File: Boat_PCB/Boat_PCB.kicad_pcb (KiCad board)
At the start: 2 copper layers, 95 x 102.5 mm, 4 parts, among them J1 Conn_02x06_Odd_Even

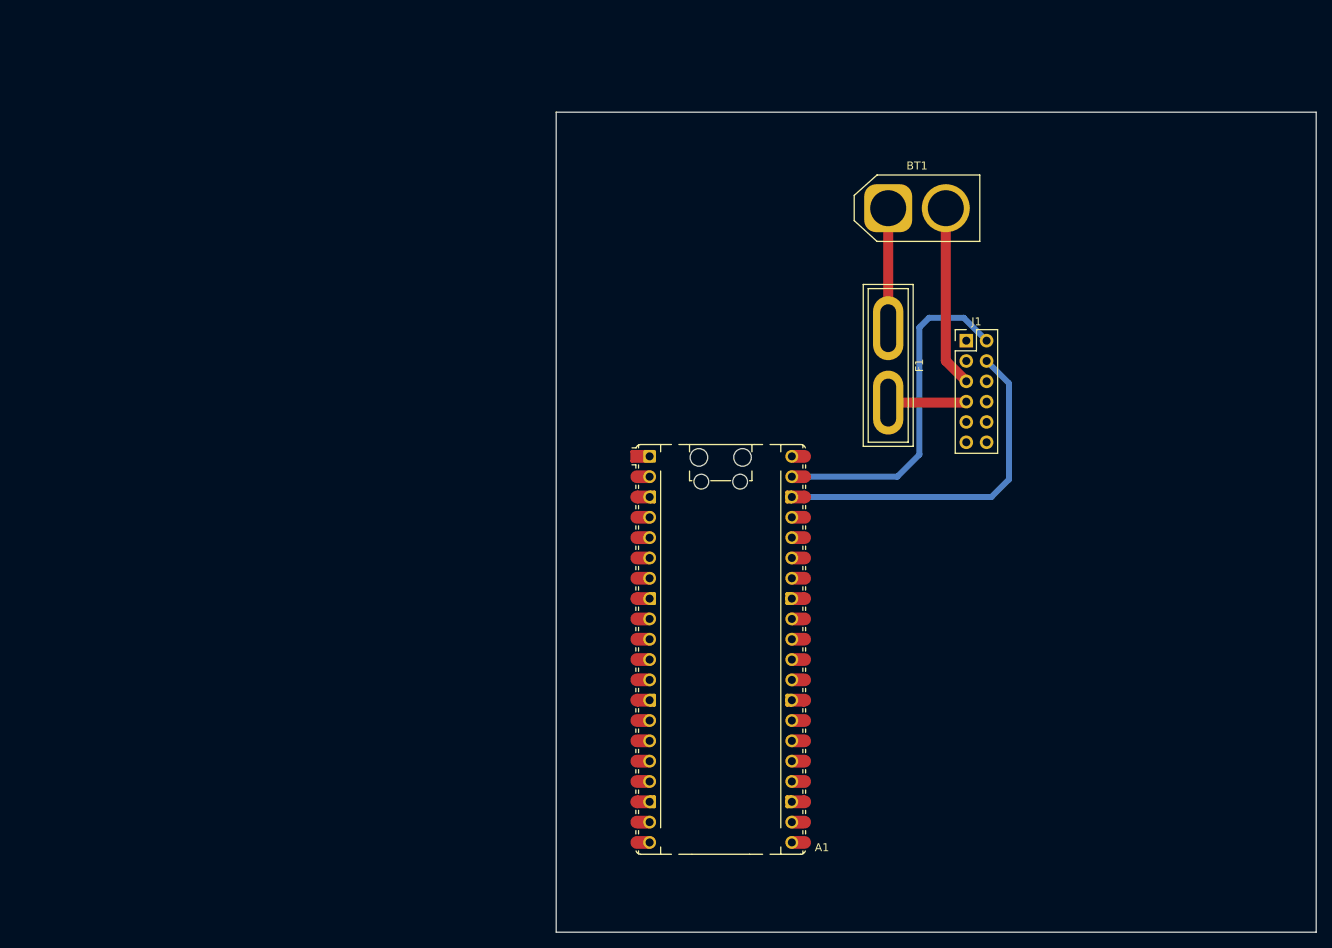
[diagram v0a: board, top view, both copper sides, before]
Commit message: Align-first steering, waypoint planner page, and M18 battery migration
Replaces proximity-boost turn logic with an align-first controller that
pivots the boat to face the next waypoint before driving forward, fixing
orbiting around waypoints. Adds a standalone waypoint planner page with a
saved-path library, wired into the command center's LOAD PATH picker and
SET HDG control. Also carries forward the three-domain Milwaukee M18
battery migration in firmware/docs and the KiCad schematic/PCB rework to
match the new divider values.

Co-Authored-By: Claude Sonnet 5 <noreply@anthropic.com>
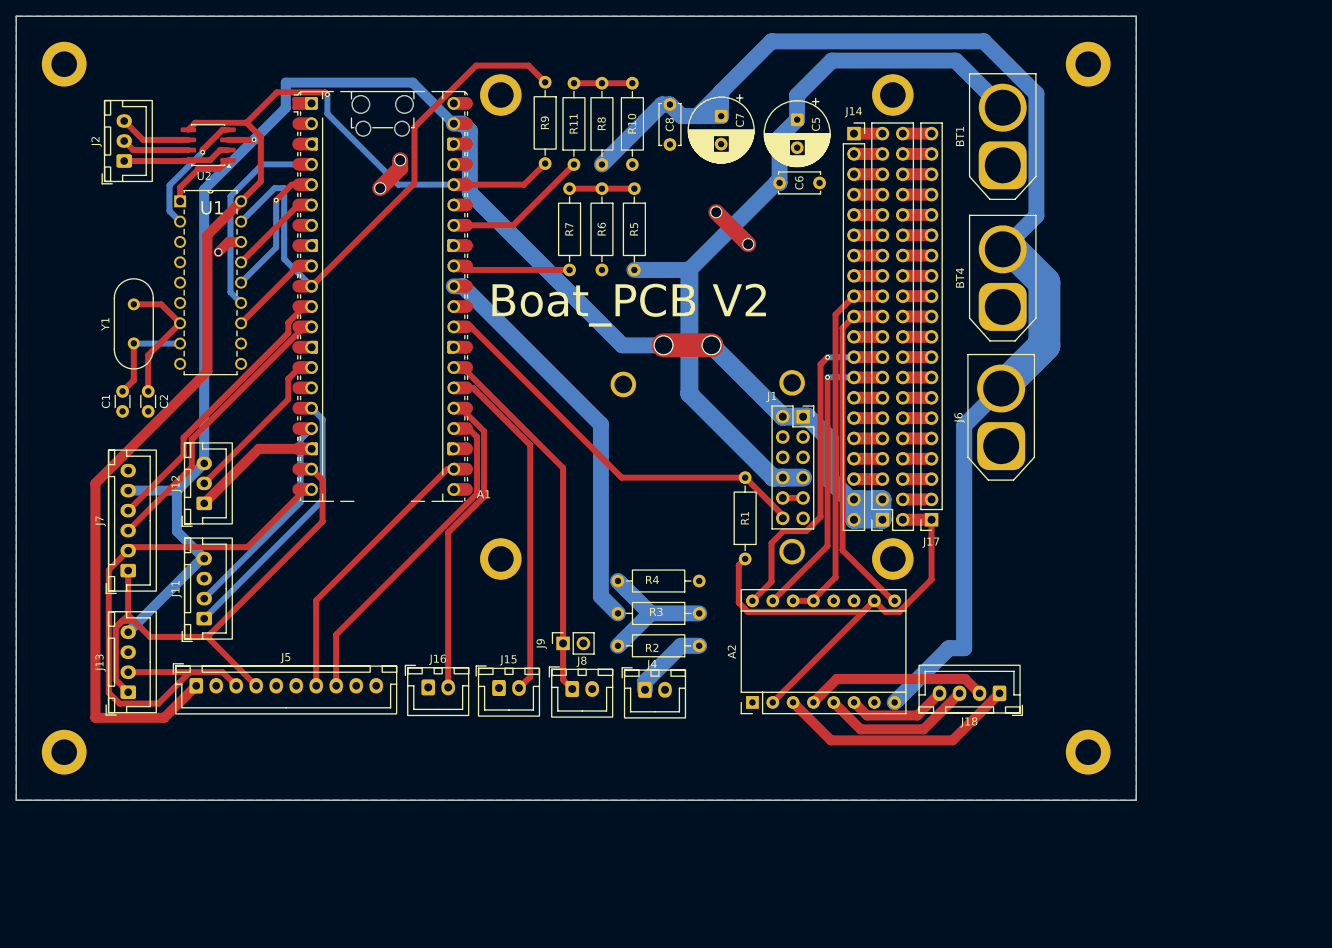
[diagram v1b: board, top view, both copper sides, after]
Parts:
- removed F1: Fuse, Fuse:Fuse_Blade_ATO_directSolder
- added A2: Pololu_Breakout_A4988, Module:Pololu_Breakout-16_15.2x20.3mm, F.Cu at (138.0, 106.8)
- added BT4: 4s, Connector_AMASS:AMASS_XT60-M_1x02_P7.20mm_Vertical, F.Cu at (169.3, 57.3)
- added C1: C, Capacitor_THT:C_Disc_D3.0mm_W1.6mm_P2.50mm, F.Cu at (59.3, 70.4)
- added C2: C, Capacitor_THT:C_Disc_D3.0mm_W1.6mm_P2.50mm, F.Cu at (62.5, 70.4)
- added C5: C_Polarized, Capacitor_THT:CP_Radial_D8.0mm_P3.50mm, F.Cu at (143.6, 33.9)
- added C6: C, Capacitor_THT:C_Disc_D5.0mm_W2.5mm_P5.00mm, F.Cu at (141.4, 41.8)
- added C7: C_Polarized, Capacitor_THT:CP_Radial_D8.0mm_P3.50mm, F.Cu at (134.1, 33.5)
- added C8: C, Capacitor_THT:C_Disc_D5.0mm_W2.5mm_P5.00mm, F.Cu at (127.7, 32.0)
- added J11: Temp + Humidity Sensor External GPIO 12,13 I2C, Connector_JST:JST_XH_B4B-XH-A_1x04_P2.50mm_Vertical, F.Cu at (69.5, 96.3)
- added J12: led GPIO 12, Connector_JST:JST_XH_B3B-XH-A_1x03_P2.50mm_Vertical, F.Cu at (69.5, 81.9)
- added J13: Temp + Humidity Sensor Internal GPIO 14,15 I2C, Connector_JST:JST_XH_B4B-XH-A_1x04_P2.50mm_Vertical, F.Cu at (60.0, 105.5)
- added J14: Conn_01x20_Socket, Connector_PinSocket_2.54mm:PinSocket_1x20_P2.54mm_Vertical, F.Cu at (150.7, 35.7)
- added J15: Hull Leak Right GPIO 20, Connector_JST:JST_XH_B2B-XH-A_1x02_P2.50mm_Vertical, F.Cu at (106.3, 105.0)
- added J16: Hull Leak Left GPIO 19, Connector_JST:JST_XH_B2B-XH-A_1x02_P2.50mm_Vertical, F.Cu at (97.5, 104.9)
- added J17: Conn_01x20_Socket, Connector_PinSocket_2.54mm:PinSocket_1x20_P2.54mm_Vertical, F.Cu at (160.4, 83.9)
- added J18: Stepper Motor, Connector_JST:JST_XH_B4B-XH-A_1x04_P2.50mm_Vertical, F.Cu at (168.9, 105.6)
- added J2: Conn_01x03_Socket, Connector_JST:JST_XH_B3B-XH-A_1x03_P2.50mm_Vertical, F.Cu at (59.5, 39.1)
- added J3: Raspberry Pi 5 connector, Module:Raspberry Pi Mounting, F.Cu at (106.6, 88.8)
- added J4: 12s Tap, Connector_JST:JST_XH_B2B-XH-A_1x02_P2.50mm_Vertical, F.Cu at (124.6, 105.2)
- added J5: IMU 14,15 I2C 17,18 RST and INT., Connector_JST:JST_XH_B10B-XH-A_1x10_P2.50mm_Vertical, F.Cu at (68.5, 104.7)
- added J6: 4s output, Connector_AMASS:AMASS_XT60-M_1x02_P7.20mm_Vertical, F.Cu at (169.1, 74.7)
- added J7: GPS + Compass GPIO 8,9 +15,14 I2C, Connector_JST:JST_XH_B6B-XH-A_1x06_P2.50mm_Vertical, F.Cu at (60.0, 90.3)
- added J8: Winch ESC GPIO 21, Connector_JST:JST_XH_B2B-XH-A_1x02_P2.50mm_Vertical, F.Cu at (115.5, 105.1)
- added J9: Winch ESC RC, Connector_PinSocket_2.54mm:PinSocket_1x02_P2.54mm_Vertical, F.Cu at (114.4, 99.4)
- added R1: R 10k, Resistor_THT:R_Axial_DIN0207_L6.3mm_D2.5mm_P10.16mm_Horizontal, F.Cu at (137.1, 88.8)
- added R10: R 18k, Resistor_THT:R_Axial_DIN0207_L6.3mm_D2.5mm_P10.16mm_Horizontal, F.Cu at (123.0, 39.5)
- added R11: R 10k, Resistor_THT:R_Axial_DIN0207_L6.3mm_D2.5mm_P10.16mm_Horizontal, F.Cu at (112.1, 29.3)
- added R2: R 220k, Resistor_THT:R_Axial_DIN0207_L6.3mm_D2.5mm_P10.16mm_Horizontal, F.Cu at (131.4, 99.7)
- added R3: R 1k, Resistor_THT:R_Axial_DIN0207_L6.3mm_D2.5mm_P10.16mm_Horizontal, F.Cu at (131.4, 95.7)
- added R4: R 13k, Resistor_THT:R_Axial_DIN0207_L6.3mm_D2.5mm_P10.16mm_Horizontal, F.Cu at (131.4, 91.6)
- added R5: R 100k, Resistor_THT:R_Axial_DIN0207_L6.3mm_D2.5mm_P10.16mm_Horizontal, F.Cu at (123.3, 42.6)
- added R6: R 30k, Resistor_THT:R_Axial_DIN0207_L6.3mm_D2.5mm_P10.16mm_Horizontal, F.Cu at (119.2, 42.6)
- added R7: R 1k, Resistor_THT:R_Axial_DIN0207_L6.3mm_D2.5mm_P10.16mm_Horizontal, F.Cu at (115.2, 42.6)
- added R8: R 100k, Resistor_THT:R_Axial_DIN0207_L6.3mm_D2.5mm_P10.16mm_Horizontal, F.Cu at (119.2, 39.5)
- added R9: R 1k, Resistor_THT:R_Axial_DIN0207_L6.3mm_D2.5mm_P10.16mm_Horizontal, F.Cu at (115.7, 39.5)
- added REF**: MountingHole_3.2mm_M3_DIN965_Pad, MountingHole:MountingHole_3.2mm_M3_DIN965_Pad, F.Cu at (180.0, 113.0)
- added REF**: MountingHole_3.2mm_M3_DIN965_Pad, MountingHole:MountingHole_3.2mm_M3_DIN965_Pad, F.Cu at (52.0, 27.0)
- added REF**: MountingHole_3.2mm_M3_DIN965_Pad, MountingHole:MountingHole_3.2mm_M3_DIN965_Pad, F.Cu at (180.0, 27.0)
- added REF**: MountingHole_3.2mm_M3_DIN965_Pad, MountingHole:MountingHole_3.2mm_M3_DIN965_Pad, F.Cu at (52.0, 113.0)
- added U1: MCP2515-I_P, MCP2515-I_P:DIP254P762X432-18, F.Cu at (74.1, 64.5)
- added U2: TJA1051T-3, Package_SO:SOIC-8_3.9x4.9mm_P1.27mm, F.Cu at (70.0, 37.1)
- added Y1: Crystal, Crystal:Crystal_HC49-4H_Vertical, F.Cu at (60.7, 61.9)
- A1: footprint Module:RaspberryPi_Pico_Common_Unspecified -> Module:Raspberry pico no antenna
- BT1: value Battery -> 3s; footprint Connector_AMASS:AMASS_XT60-F_1x02_P7.20mm_Vertical -> Connector_AMASS:AMASS_XT60-M_1x02_P7.20mm_Vertical
- J1: footprint Connector_PinHeader_2.54mm:PinHeader_2x06_P2.54mm_Vertical -> Module:Pololu 36v5vstepdown
- moved A1 61.1 mm to (91.8, 56.0)
- moved J1 22.4 mm to (143.0, 66.8)
- moved BT1 15.3 mm to (169.3, 39.6), turned to 90 degrees
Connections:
- A1 pad 10: unconnected-(A1-GPIO7-Pad10) -> Net-(A1-GPIO7)
- A1 pad 11: unconnected-(A1-GPIO8-Pad11) -> Net-(A1-GPIO8)
- A1 pad 12: unconnected-(A1-GPIO9-Pad12) -> Net-(A1-GPIO9)
- A1 pad 13: Net-(J1-Pin_4) -> GND
- A1 pad 14: unconnected-(A1-GPIO10-Pad14) -> Net-(A1-GPIO10)
- A1 pad 16: unconnected-(A1-GPIO12-Pad16) -> Net-(A1-GPIO12)
- A1 pad 17: unconnected-(A1-GPIO13-Pad17) -> Net-(A1-GPIO13)
- A1 pad 18: Net-(J1-Pin_4) -> GND
- A1 pad 19: unconnected-(A1-GPIO14-Pad19) -> Net-(A1-GPIO14)
- A1 pad 20: unconnected-(A1-GPIO15-Pad20) -> Net-(A1-GPIO15)
- A1 pad 22: unconnected-(A1-GPIO17-Pad22) -> Net-(A1-GPIO17)
- A1 pad 23: Net-(J1-Pin_4) -> GND
- A1 pad 24: unconnected-(A1-GPIO18-Pad24) -> Net-(A1-GPIO18)
- A1 pad 25: unconnected-(A1-GPIO19-Pad25) -> Net-(A1-GPIO19)
- A1 pad 26: unconnected-(A1-GPIO20-Pad26) -> Net-(A1-GPIO20)
- A1 pad 27: unconnected-(A1-GPIO21-Pad27) -> Net-(A1-GPIO21)
- A1 pad 28: Net-(J1-Pin_4) -> GND
- A1 pad 29: unconnected-(A1-GPIO22-Pad29) -> Net-(A1-GPIO22)
- A1 pad 3: Net-(J1-Pin_4) -> GND
- A1 pad 31: unconnected-(A1-GPIO26_ADC0-Pad31) -> Net-(A1-GPIO26_ADC0)
- A1 pad 32: unconnected-(A1-GPIO27_ADC1-Pad32) -> Net-(A1-GPIO27_ADC1)
- A1 pad 34: unconnected-(A1-GPIO28_ADC2-Pad34) -> Net-(A1-GPIO28_ADC2)
- A1 pad 36: unconnected-(A1-3V3-Pad36) -> Net-(A1-3V3)
- A1 pad 38: Net-(J1-Pin_4) -> GND
- A1 pad 4: unconnected-(A1-GPIO2-Pad4) -> Net-(A1-GPIO2)
- A1 pad 5: unconnected-(A1-GPIO3-Pad5) -> Net-(A1-GPIO3)
- A1 pad 6: unconnected-(A1-GPIO4-Pad6) -> Net-(A1-GPIO4)
- A1 pad 7: unconnected-(A1-GPIO5-Pad7) -> GND
- A1 pad 8: Net-(J1-Pin_4) -> GND
- A1 pad 9: unconnected-(A1-GPIO6-Pad9) -> Net-(A1-GPIO6)
- BT1 pad 1: Net-(BT1-+) -> GND
- J1 pad 1: unconnected-(J1-Pin_1-Pad1) -> Net-(A1-VSYS)
- J1 pad 10: unconnected-(J1-Pin_10-Pad10) -> Net-(J1-Pin_10)
- J1 pad 12: unconnected-(J1-Pin_12-Pad12) -> Net-(A1-GPIO22)
- J1 pad 3: unconnected-(J1-Pin_3-Pad3) -> GND
- J1 pad 4: Net-(J1-Pin_4) -> GND
- J1 pad 5: Net-(BT1--) -> GND
- J1 pad 6: unconnected-(J1-Pin_6-Pad6) -> GND
- J1 pad 7: Net-(J1-Pin_7) -> Net-(BT1--)
- J1 pad 8: unconnected-(J1-Pin_8-Pad8) -> Net-(BT1--)
- J1 pad 9: unconnected-(J1-Pin_9-Pad9) -> Net-(J1-Pin_10)
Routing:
- net Net-(A1-VSYS): track 43.1 -> 210.7 mm, vias 0 -> 3
- net Net-(A2-VMOT): track 0.00 -> 160.1 mm
- net Net-(A1-3V3): track 0.00 -> 151.7 mm, vias 0 -> 1
- net Net-(BT1--): track 22.7 -> 98.5 mm
- net Net-(A1-GPIO15): track 0.00 -> 70.6 mm
- net Net-(A1-GPIO7): track 0.00 -> 66.4 mm
- net Net-(A1-GPIO14): track 0.00 -> 66.3 mm
- net Net-(A2-MS1): track 0.00 -> 62.2 mm
- net Net-(A1-GPIO22): track 0.00 -> 51.3 mm
- net GND: track 0.00 -> 50.5 mm, vias 0 -> 5
- net Net-(A1-GPIO26_ADC0): track 0.00 -> 50.1 mm
- net Net-(A1-GPIO21): track 0.00 -> 47.4 mm
- net Net-(A2-~{RESET}): track 0.00 -> 46.3 mm
- net Net-(J1-Pin_4): track 44.0 -> 0.00 mm
- net Net-(A1-GPIO20): track 0.00 -> 43.5 mm
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- added copper zone on B.Cu, net GND
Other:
- board size 95 x 102.5 mm -> 140 x 98 mm
- board text added: "Boat_PCB V2"
